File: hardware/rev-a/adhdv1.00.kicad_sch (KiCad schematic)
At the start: 4 parts

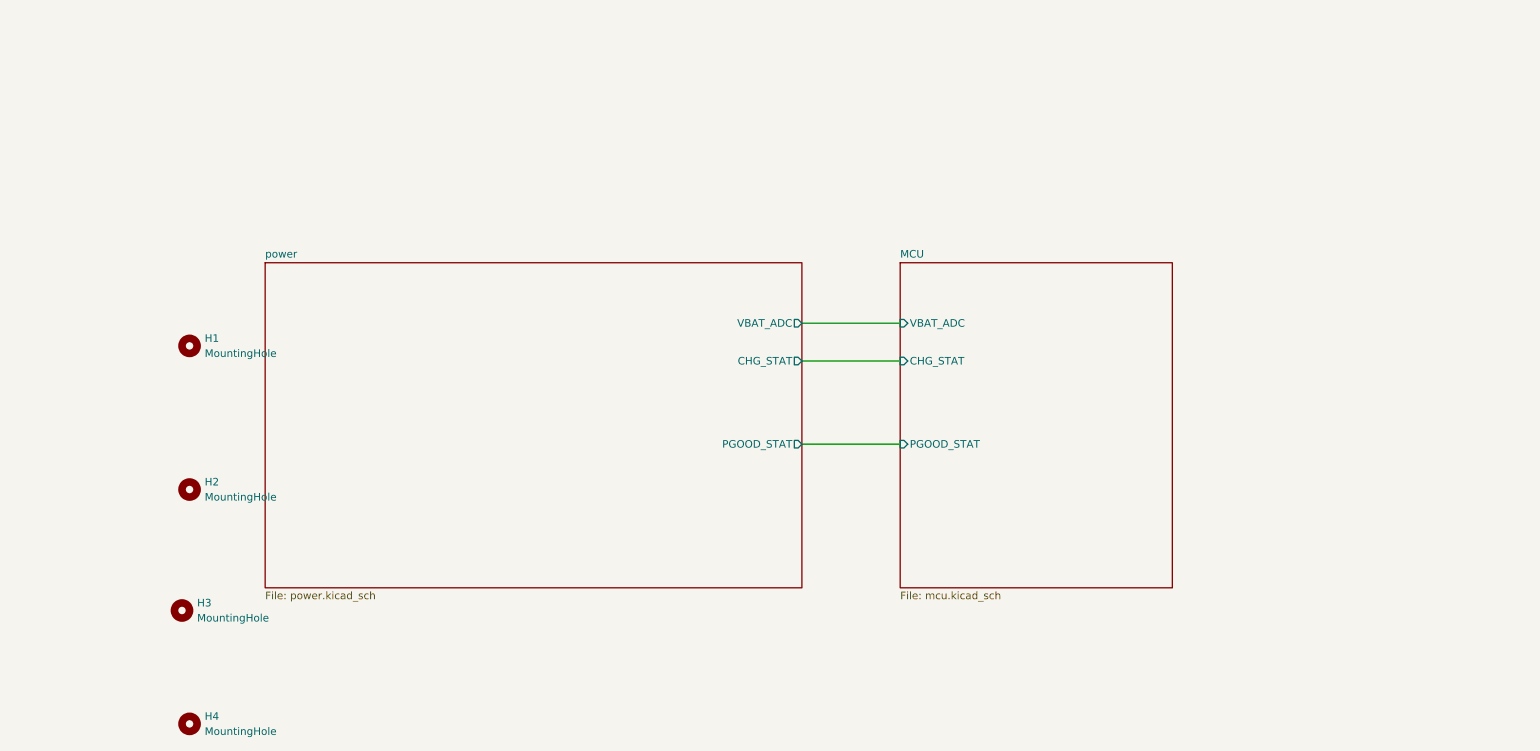
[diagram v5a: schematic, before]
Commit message: format schematic to fit convention, replace SWD header with 2x5
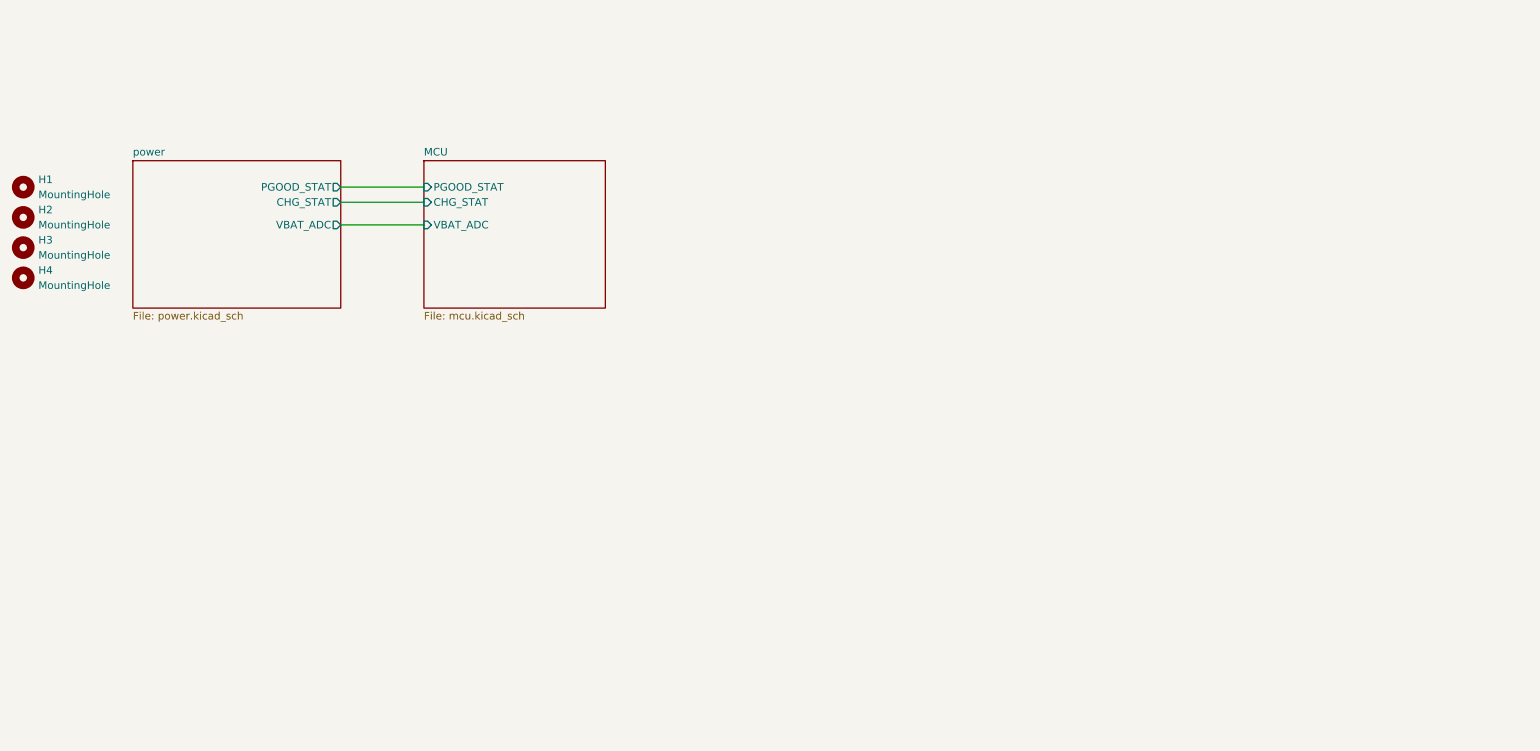
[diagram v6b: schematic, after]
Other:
- moved on the sheet: H1, H2, H3, H4
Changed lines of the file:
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@@
 	(wire
 		(pts
-			(xy 157.48 96.52) (xy 173.99 96.52)
+			(xy 80.01 59.69) (xy 93.98 59.69)
 		)
 		(stroke
@@
 	(wire
 		(pts
-			(xy 157.48 82.55) (xy 173.99 82.55)
+			(xy 80.01 53.34) (xy 93.98 53.34)
 		)
 		(stroke
@@
 	(wire
 		(pts
-			(xy 157.48 76.2) (xy 173.99 76.2)
+			(xy 80.01 55.88) (xy 93.98 55.88)
 		)
 		(stroke
@@
 	(symbol
 		(lib_id "Mechanical:MountingHole")
-		(at 54.61 104.14 0)
+		(at 26.67 58.42 0)
 		(unit 1)
 		(exclude_from_sim no)
@@
 		(fields_autoplaced yes)
 		(property "Reference" "H2"
-			(at 57.15 102.8699 0)
+			(at 29.21 57.1499 0)
 			(effects
 				(font
@@
 		)
 		(property "Value" "MountingHole"
-			(at 57.15 105.4099 0)
+			(at 29.21 59.6899 0)
 			(effects
 				(font
@@
 		)
 		(property "Footprint" "MountingHole:MountingHole_2.2mm_M2_Pad"
-			(at 54.61 104.14 0)
+			(at 26.67 58.42 0)
 			(effects
 				(font
@@
 		)
 		(property "Datasheet" "~"
-			(at 54.61 104.14 0)
+			(at 26.67 58.42 0)
 			(effects
 				(font
@@
 		)
 		(property "Description" "Mounting Hole without connection"
-			(at 54.61 104.14 0)
+			(at 26.67 58.42 0)
 			(effects
 				(font
@@
 	(symbol
 		(lib_id "Mechanical:MountingHole")
-		(at 53.34 124.46 0)
+		(at 26.67 63.5 0)
 		(unit 1)
 		(exclude_from_sim no)
@@
 		(on_board yes)
 		(dnp no)
-		(fields_autoplaced yes)
 		(property "Reference" "H3"
-			(at 55.88 123.1899 0)
+			(at 29.21 62.2299 0)
 			(effects
 				(font
@@
 		)
 		(property "Value" "MountingHole"
-			(at 55.88 125.7299 0)
+			(at 29.21 64.7699 0)
 			(effects
 				(font
@@
 		)
 		(property "Footprint" "MountingHole:MountingHole_2.2mm_M2_Pad"
-			(at 53.34 124.46 0)
+			(at 26.67 63.5 0)
 			(effects
 				(font
@@
 		)
 		(property "Datasheet" "~"
-			(at 53.34 124.46 0)
+			(at 26.67 63.5 0)
 			(effects
 				(font
@@
 		)
 		(property "Description" "Mounting Hole without connection"
-			(at 53.34 124.46 0)
+			(at 26.67 63.5 0)
 			(effects
 				(font
@@
 	(symbol
 		(lib_id "Mechanical:MountingHole")
-		(at 54.61 80.01 0)
+		(at 26.67 53.34 0)
 		(unit 1)
 		(exclude_from_sim no)
@@
 		(fields_autoplaced yes)
 		(property "Reference" "H1"
-			(at 57.15 78.7399 0)
+			(at 29.21 52.0699 0)
 			(effects
 				(font
@@
 		)
 		(property "Value" "MountingHole"
-			(at 57.15 81.2799 0)
+			(at 29.21 54.6099 0)
 			(effects
 				(font
@@
 		)
 		(property "Footprint" "MountingHole:MountingHole_2.2mm_M2_Pad"
-			(at 54.61 80.01 0)
+			(at 26.67 53.34 0)
 			(effects
 				(font
@@
 		)
 		(property "Datasheet" "~"
-			(at 54.61 80.01 0)
+			(at 26.67 53.34 0)
 			(effects
 				(font
@@
 		)
 		(property "Description" "Mounting Hole without connection"
-			(at 54.61 80.01 0)
+			(at 26.67 53.34 0)
 			(effects
 				(font
@@
 	(symbol
 		(lib_id "Mechanical:MountingHole")
-		(at 54.61 143.51 0)
+		(at 26.67 68.58 0)
 		(unit 1)
 		(exclude_from_sim no)
@@
 		(fields_autoplaced yes)
 		(property "Reference" "H4"
-			(at 57.15 142.2399 0)
+			(at 29.21 67.3099 0)
 			(effects
 				(font
@@
 		)
 		(property "Value" "MountingHole"
-			(at 57.15 144.7799 0)
+			(at 29.21 69.8499 0)
 			(effects
 				(font
@@
 		)
 		(property "Footprint" "MountingHole:MountingHole_2.2mm_M2_Pad"
-			(at 54.61 143.51 0)
+			(at 26.67 68.58 0)
 			(effects
 				(font
@@
 		)
 		(property "Datasheet" "~"
-			(at 54.61 143.51 0)
+			(at 26.67 68.58 0)
 			(effects
 				(font
@@
 		)
 		(property "Description" "Mounting Hole without connection"
-			(at 54.61 143.51 0)
+			(at 26.67 68.58 0)
 			(effects
 				(font
@@
 	)
 	(sheet
-		(at 173.99 66.04)
-		(size 45.72 54.61)
+		(at 93.98 48.895)
+		(size 30.48 24.765)
 		(exclude_from_sim no)
 		(in_bom yes)
@@
 		)
 		(property "Sheetname" "MCU"
-			(at 173.99 65.3284 0)
+			(at 93.98 48.1834 0)
 			(effects
 				(font
@@
 		)
 		(property "Sheetfile" "mcu.kicad_sch"
-			(at 173.99 121.2346 0)
+			(at 93.98 74.2446 0)
 			(effects
 				(font
@@
 		)
 		(pin "CHG_STAT" input
-			(at 173.99 82.55 180)
+			(at 93.98 55.88 180)
 			(effects
 				(font
@@
 		)
 		(pin "PGOOD_STAT" input
-			(at 173.99 96.52 180)
+			(at 93.98 53.34 180)
 			(effects
 				(font
@@
 		)
 		(pin "VBAT_ADC" input
-			(at 173.99 76.2 180)
+			(at 93.98 59.69 180)
 			(effects
 				(font
@@
 	)
 	(sheet
-		(at 67.31 66.04)
-		(size 90.17 54.61)
+		(at 45.085 48.895)
+		(size 34.925 24.765)
 		(exclude_from_sim no)
 		(in_bom yes)
@@
 		)
 		(property "Sheetname" "power"
-			(at 67.31 65.3284 0)
+			(at 45.085 48.1834 0)
 			(effects
 				(font
@@
 		)
 		(property "Sheetfile" "power.kicad_sch"
-			(at 67.31 121.2346 0)
+			(at 45.085 74.2446 0)
 			(effects
 				(font
@@
 		)
 		(pin "VBAT_ADC" output
-			(at 157.48 76.2 0)
+			(at 80.01 59.69 0)
 			(effects
 				(font
@@
 		)
 		(pin "CHG_STAT" output
-			(at 157.48 82.55 0)
+			(at 80.01 55.88 0)
 			(effects
 				(font
@@
 		)
 		(pin "PGOOD_STAT" output
-			(at 157.48 96.52 0)
-			(effects
-				(font
+			(at 80.01 53.34 0)
+			(effects
+				(font
